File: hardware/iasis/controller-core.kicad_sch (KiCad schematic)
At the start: 39 parts, among them J1101 SWD debug, SW1101 PTS645SL50SMTR92LFS, SW1102 PTS645SL50SMTR92LFS, U1101 RP2354B, Y1101 ABM8-272-T3

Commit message: Keep the switch jumper flag in the symbol
Update PCB from Schematic sets each footprint's duplicate-pad jumper flag
from its symbol, so the flag set only on the SW1101, SW1102 and SW1171
footprints would not have survived the next update from the stock
Switch:SW_Push. The switches now use Iasis:PTS645SL50SMTR92LFS, SW_Push with
duplicate pin numbers marked as jumpers, and the netlist carries the flag to
the footprints.

The footprints stay stock. Update Footprints from Library takes the
library's flag, so after refreshing them DRC reports the three pads
unconnected until the next update from the schematic.

ERC is unchanged; DRC is clean with schematic parity.
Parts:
- SW1101, SW1102: symbol Switch:SW_Push -> Iasis:PTS645SL50SMTR92LFS
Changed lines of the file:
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@@
 	)
 	(symbol
-		(lib_id "Switch:SW_Push")
+		(lib_id "Iasis:PTS645SL50SMTR92LFS")
 		(at 88.9 231.14 270)
 		(unit 1)
@@
 	)
 	(symbol
-		(lib_id "Switch:SW_Push")
+		(lib_id "Iasis:PTS645SL50SMTR92LFS")
 		(at 114.3 231.14 270)
 		(unit 1)

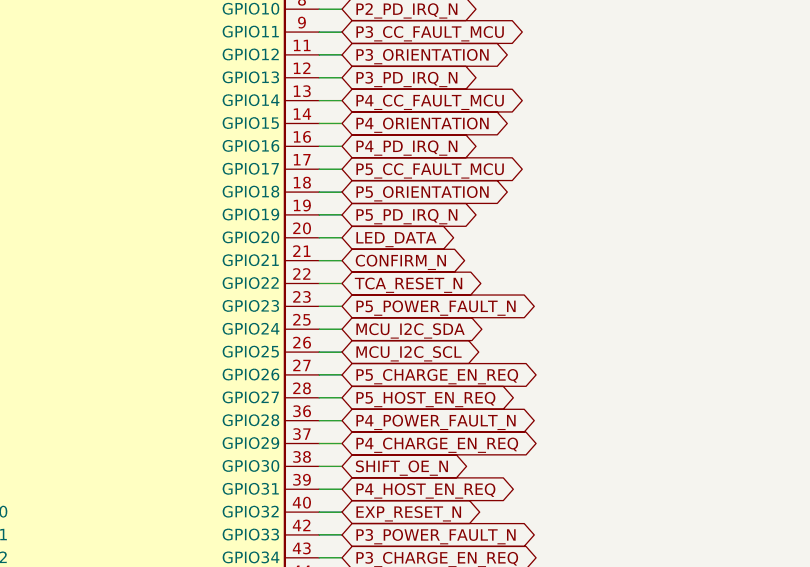
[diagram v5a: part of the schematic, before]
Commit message: fix: correct core power and recovery circuitry
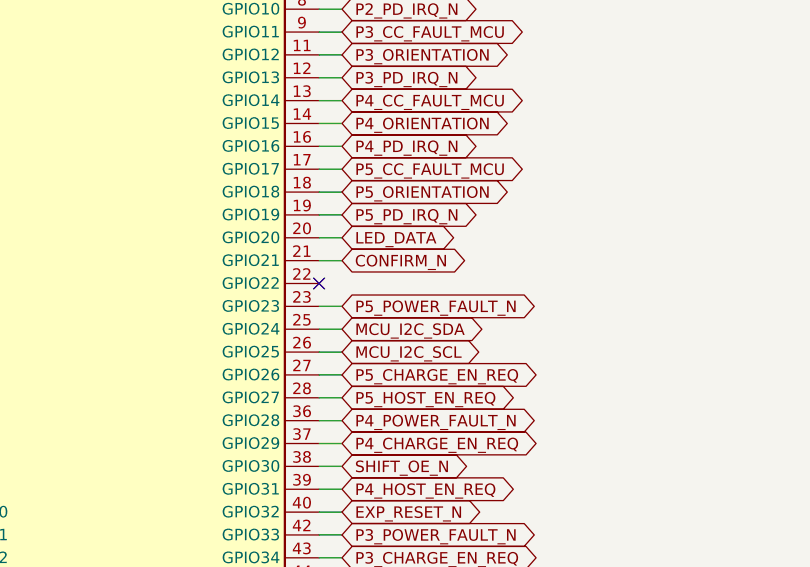
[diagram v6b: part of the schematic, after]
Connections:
- net TCA_RESET_N: no longer names the net of U1101.22 (GPIO22)
- no-connect marks 6 -> 7
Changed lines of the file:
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@@
+	)
+	(no_connect
+		(at 228.6 160.02)
 	)
 	(no_connect
@@
 	(wire
 		(pts
-			(xy 228.6 160.02) (xy 231.14 160.02)
-		)
-		(stroke
-			(width 0)
-			(type default)
-		)
-	)
-	(wire
-		(pts
 			(xy 228.6 147.32) (xy 231.14 147.32)
 		)
@@
 			(hide yes)
 			(show_name no)
-			(do_not_autoplace no)
-			(effects
-				(font
-					(size 1.27 1.27)
-				)
-			)
-		)
-	)
-	(global_label "TCA_RESET_N"
-		(shape bidirectional)
-		(at 231.14 160.02 0)
-		(effects
-			(font
-				(size 1.27 1.27)
-			)
-			(justify left)
-		)
-		(property "Intersheetrefs" "${INTERSHEET_REFS}"
-			(at 231.14 160.02 0)
-			(hide yes)
-			(show_name no)
